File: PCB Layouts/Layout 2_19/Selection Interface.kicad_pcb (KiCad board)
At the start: 4 copper layers, 107.5 x 80 mm, 87 parts

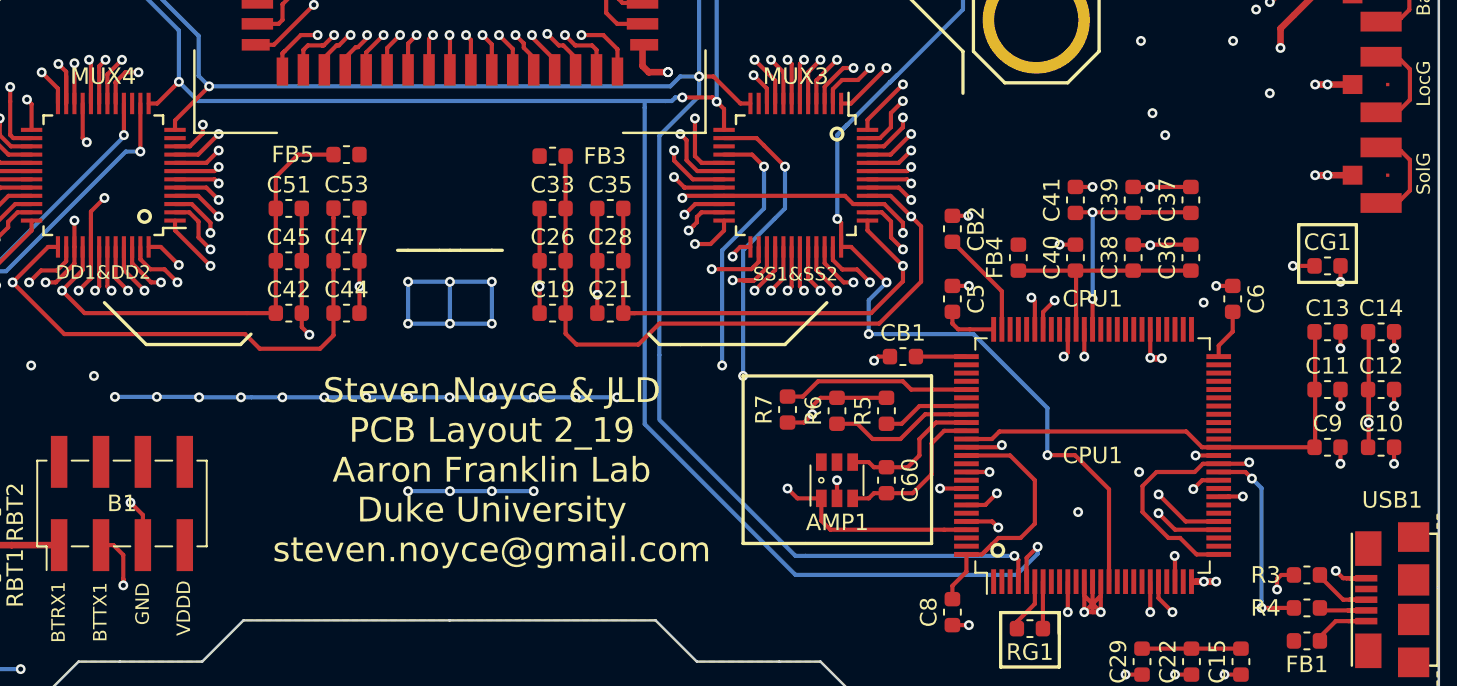
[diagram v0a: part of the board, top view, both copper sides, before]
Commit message: Slight tweaks to Layout 2_19 (removed unnecessary Gate capacitor, compressed some BT signal wiring)
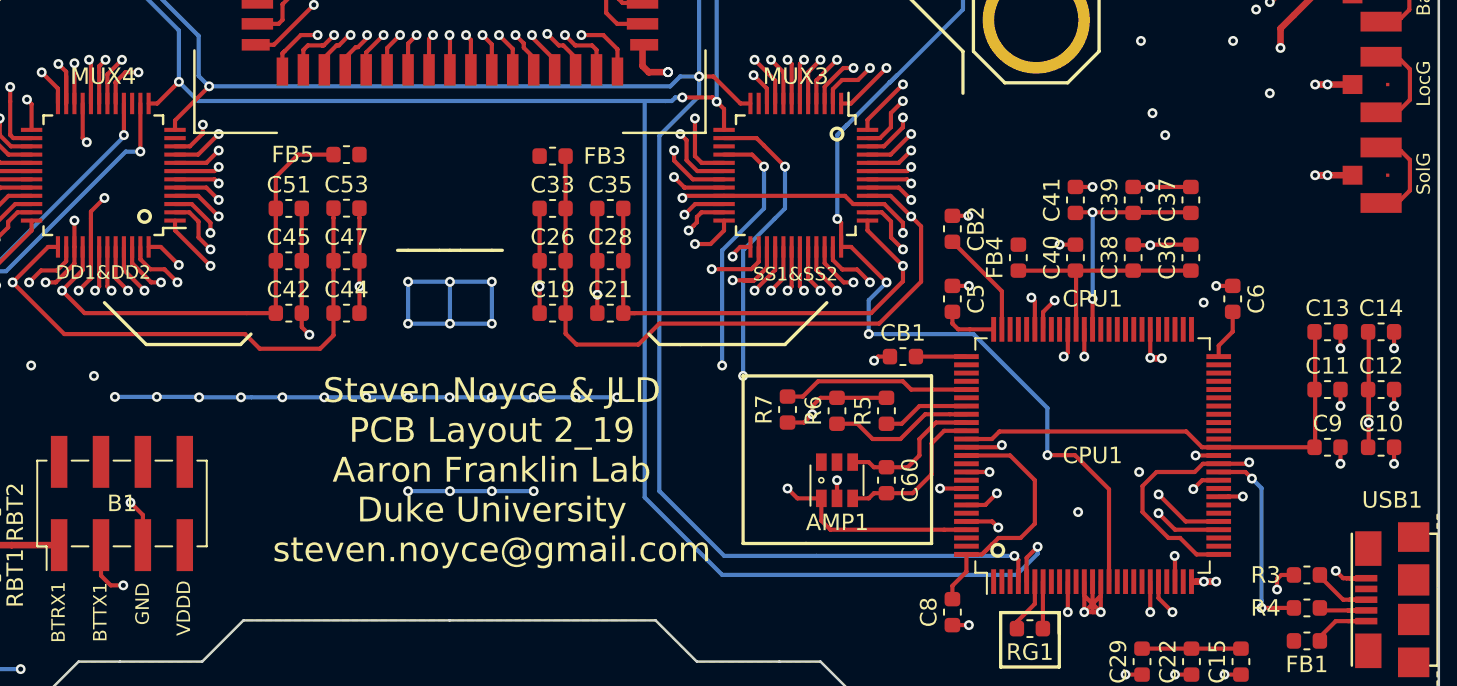
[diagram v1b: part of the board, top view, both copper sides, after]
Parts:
- removed CG1: 1pF, Capacitor_SMD:C_0603_1608Metric
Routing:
- net I2C0_SCL: track 182.4 -> 185.1 mm
- net I2C0_SDA: track 193.2 -> 195.8 mm
- net Gate: track 58.5 -> 57.2 mm, vias 5 -> 4
- net GND: track 429.3 -> 428.4 mm, vias 165 -> 164
- net BT1_TX: track 81.9 -> 81.1 mm
